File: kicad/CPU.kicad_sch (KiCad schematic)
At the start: 49 parts, among them SW1 SW_Push, U10 MC34063AD, U11 LD1117S33TR_SOT223, U4 MC34063AD, U5 STM32F303CBTx, X1 8 MHz

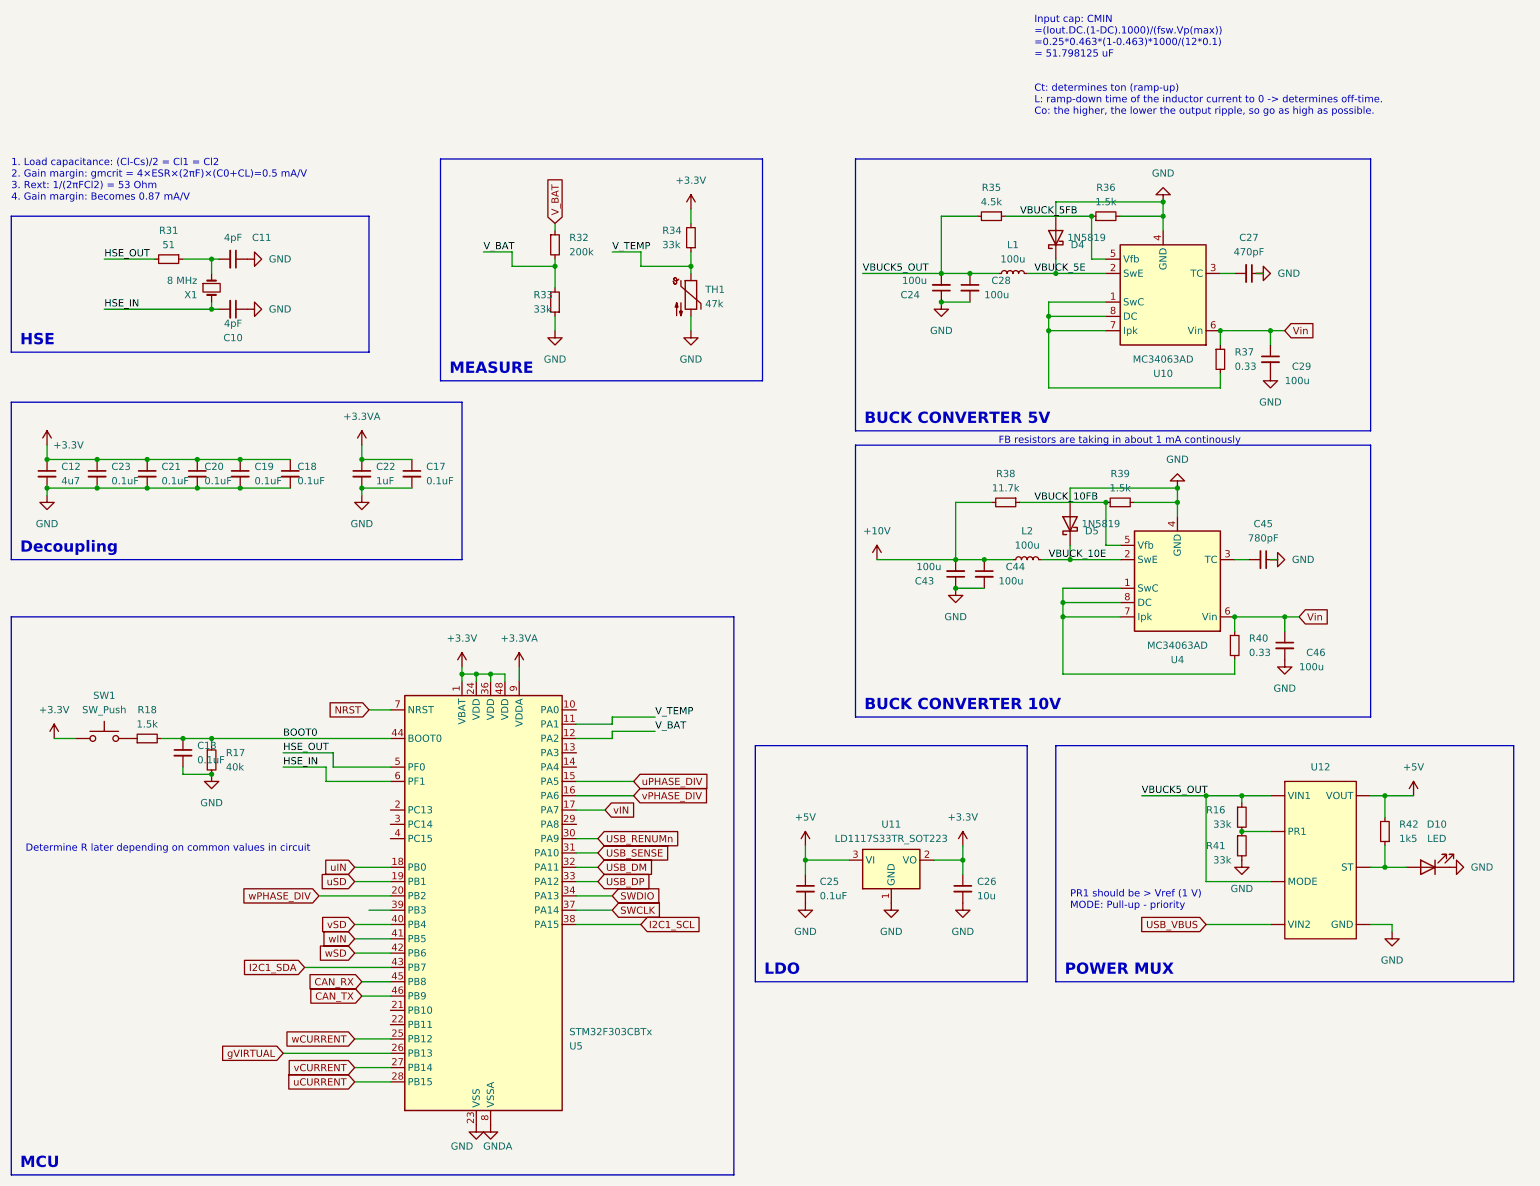
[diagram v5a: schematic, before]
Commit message: [kicad] completed resistor and capacitor BOM, added footprints, streamlined the resistance and capacitance values | TODO: find new crystal, add footprint for CAN driver + button, check IC-footprints [simulations] adapted the simulations according to changes in the schematic [scripts] Added warning for HP 0.33 ohm resistor
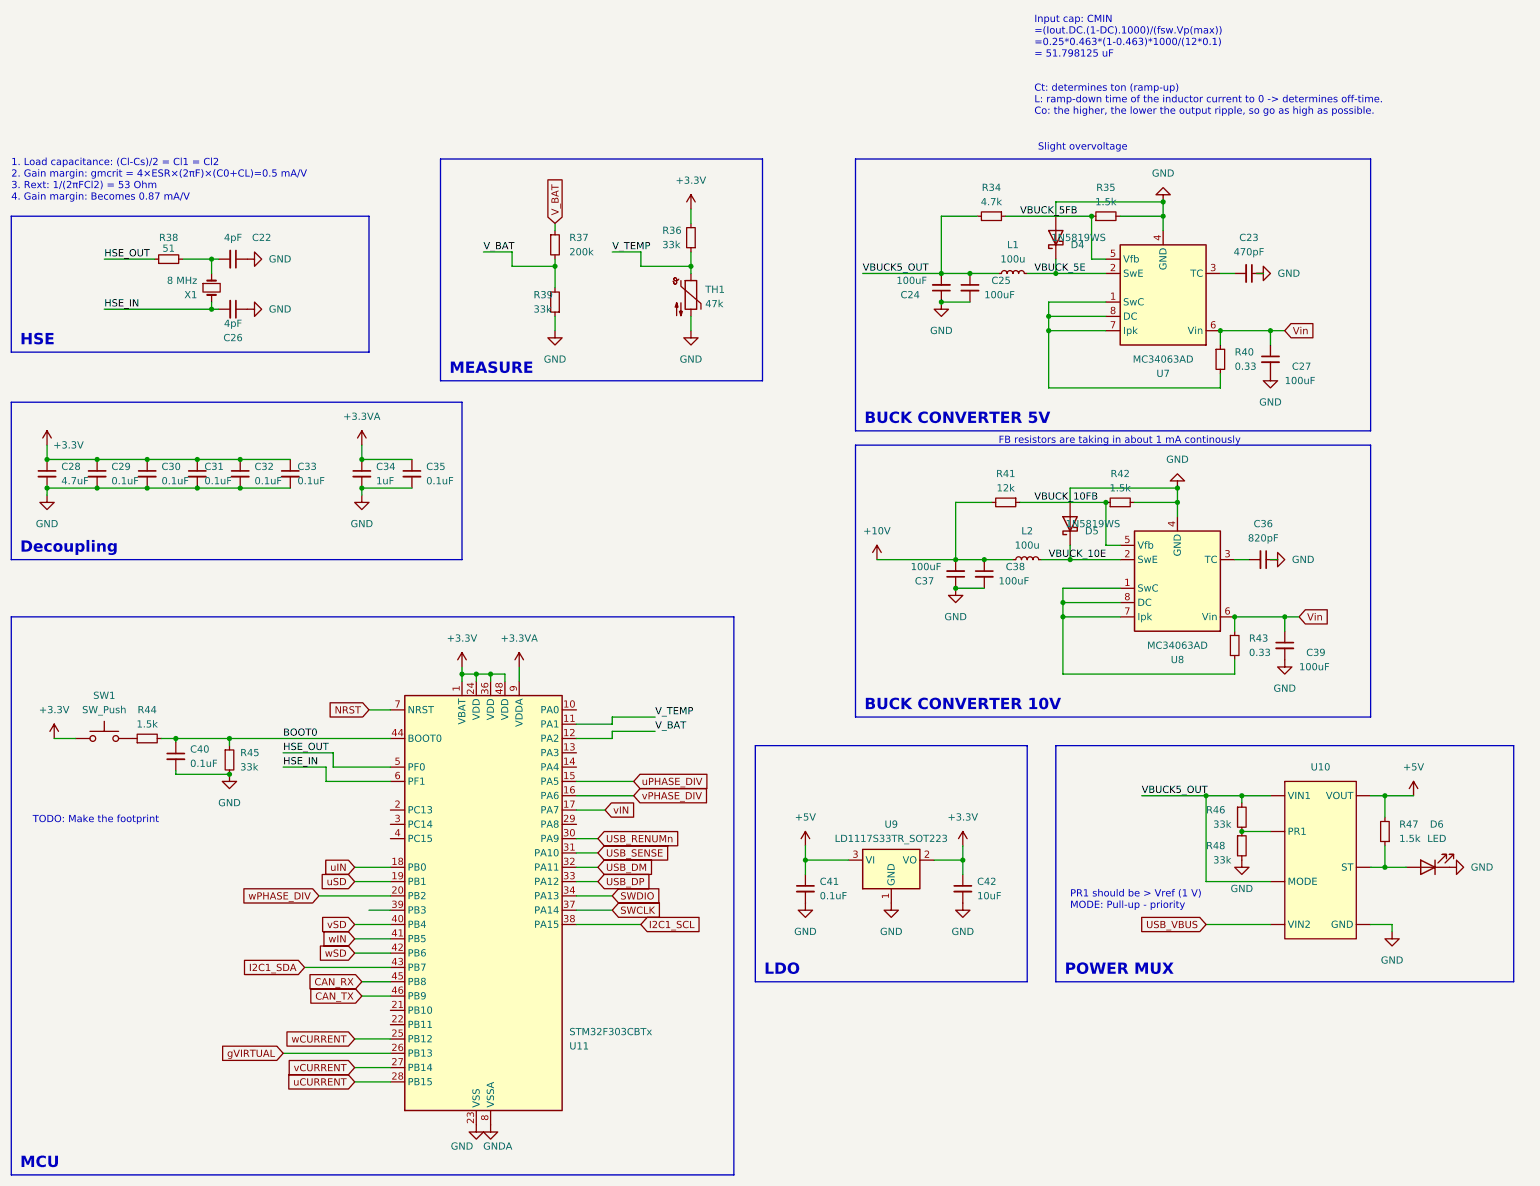
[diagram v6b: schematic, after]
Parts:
- removed R31: 51, Resistor_SMD:R_0805_2012Metric, symbol Device:R_Small
- removed R39: 1.5k, symbol Device:R_Small
- added R38: 51, Resistor_SMD:R_1206_3216Metric, symbol Device:R_Small
- added R42: 1.5k, Resistor_SMD:R_0805_2012Metric, symbol Device:R_Small
- C22: renamed from C11; footprint (none) -> Capacitor_SMD:C_0603_1608Metric; MFR.Part (none) -> CL10C040CB8NNNC; jlcpcb (none) -> C307494
- C23: renamed from C27; footprint Capacitor_SMD:C_0603_1608Metric -> Capacitor_SMD:C_0805_2012Metric; MFR.Part (none) -> 0805B471K500NT; jlcpcb (none) -> C1743
- C24: value 100u -> 100uF; MFR.Part (none) -> CA55-B6R3M107T; jlcpcb (none) -> C568913
- C25: renamed from C28; value 100u -> 100uF; MFR.Part (none) -> CA55-B6R3M107T; jlcpcb (none) -> C568913
- C26: renamed from C10; footprint (none) -> Capacitor_SMD:C_0603_1608Metric; MFR.Part (none) -> CL10C040CB8NNNC; jlcpcb (none) -> C307494
- C27: renamed from C29; value 100u -> 100uF; MFR.Part (none) -> CA55-B6R3M107T; jlcpcb (none) -> C568913
- C28: renamed from C12; value 4u7 -> 4.7uF; JLCPCB C19666 -> (none); jlcpcb (none) -> C19666
- C34: renamed from C22; jlcpcb (none) -> C1848; jlpcb C1848 -> (none)
- C36: renamed from C45; value 780pF -> 820pF; footprint Capacitor_SMD:C_0603_1608Metric -> Capacitor_SMD:C_0805_2012Metric; MFR.Part (none) -> CL21B821KBANNNC; jlcpcb (none) -> C296722
- C37: renamed from C43; value 100u -> 100uF; MFR.Part (none) -> CA55-B6R3M107T; jlcpcb (none) -> C568913
- C38: renamed from C44; value 100u -> 100uF; MFR.Part (none) -> CA55-B6R3M107T; jlcpcb (none) -> C568913
- C39: renamed from C46; value 100u -> 100uF; MFR.Part (none) -> CA55-B6R3M107T; jlcpcb (none) -> C568913
- C42: renamed from C26; value 10u -> 10uF; footprint (none) -> Capacitor_SMD:C_0402_1005Metric; jlcpcb (none) -> C15525
- D4, D5: value 1N5819 -> 1N5819WS; footprint Diode_THT:D_DO-41_SOD81_P10.16mm_Horizontal -> Diode_SMD:D_SOD-323; MFR.Part (none) -> 1N5819WS; jlcpcb (none) -> C191023
- D6: renamed from D10; MFR.Part (none) -> BZ-C0805-Y2-E1; jlcpcb (none) -> C2833070
- R34: renamed from R35; value 4.5k -> 4.7k; footprint (none) -> Resistor_SMD:R_0805_2012Metric; MFR.Part (none) -> 0805W8F4701T5E; jlcpcb (none) -> C17673
- R35: renamed from R36; footprint (none) -> Resistor_SMD:R_0805_2012Metric; jlcpcb (none) -> C4310
- R40: renamed from R37; footprint (none) -> Resistor_SMD:R_2512_6332Metric; MFR.Part (none) -> 25121WF330LT4E; jlcpcb (none) -> C25468
- R41: renamed from R38; value 11.7k -> 12k; footprint (none) -> Resistor_SMD:R_0603_1608Metric; MFR.Part (none) -> 0603WAF1202T5E; jlcpcb (none) -> C22790
- R43: renamed from R40; footprint (none) -> Resistor_SMD:R_2512_6332Metric; MFR.Part (none) -> 25121WF330LT4E; jlcpcb (none) -> C25468
- R44: renamed from R18; footprint (none) -> Resistor_SMD:R_0805_2012Metric; jlcpcb (none) -> C4310
- R45: renamed from R17; value 40k -> 33k; footprint (none) -> Resistor_SMD:R_0603_1608Metric; jlcpcb (none) -> C4216
- R46: renamed from R16; footprint (none) -> Resistor_SMD:R_0603_1608Metric; jlcpcb (none) -> C4216
- R47: renamed from R42; value 1k5 -> 1.5k; footprint (none) -> Resistor_SMD:R_0805_2012Metric; jlcpcb (none) -> C4310
- R48: renamed from R41; footprint (none) -> Resistor_SMD:R_0603_1608Metric; jlcpcb (none) -> C4216
- SW1: MFR.Part (none) -> 5.8 ZSGT; jlcpcb (none) -> C2681587
- U10: renamed from U12; footprint (none) -> Package_TO_SOT_SMD:SOT-583-8; MFR.Part (none) -> TPS2116DRLR; jlcpcb (none) -> C3235557
- renumbered C23 to C29, C21 to C30, C20 to C31, C19 to C32, C18 to C33, C17 to C35, C13 to C40, C25 to C41, R34 to R36, R32 to R37, R33 to R39, U5 to U11, U10 to U7, U4 to U8, U11 to U9
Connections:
- net GND: now also R42.2
- net HSE_OUT: now also R38.1
- net VBUCK_10FB: now also R42.1
- net at C22.2, X1.1: now also R38.2
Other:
- note added: "Slight overvoltage"
- note added: "TODO: Make the footprint"
- note removed: "Determine R later depending on common values in circuit"
- moved on the sheet: C40, R45

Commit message: [kicad] Added oscillator and relevant surrounding circuitry [scripts] Added resonator calculation
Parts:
- C22, C26: value 4pF -> 20pF; MFR.Part CL10C040CB8NNNC -> CL10C200JB81PNC; jlcpcb C307494 -> C346210
- R38: value 51 -> 0; footprint Resistor_SMD:R_1206_3216Metric -> Resistor_SMD:R_0402_1005Metric; JLCPCB (none) -> C17168; MFR.Part 1206W4F510JT5E -> 0402WGF0000TCE; jlcpcb C18019 -> (none)
- X1: footprint (none) -> Crystal:Crystal_SMD_3225-4Pin_3.2x2.5mm; Component ABLS-8.000MHZ-20-B-3-H-T -> (none); MFR.Part (none) -> 7325-0800A2010-00; jlcpcb (none) -> C389817
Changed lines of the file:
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@@
+    )
+  )
+  (symbol (lib_id "Device:C_Small") (at 53.34 33.02 270) (unit 1)
+    (in_bom yes) (on_board yes) (dnp no)
+    (property "Reference" "C22" (at 53.34 38.1 90)
+      (effects (font (size 1.27 1.27)))
+    )
+    (property "Value" "20pF" (at 53.34 35.56 90)
+      (effects (font (size 1.27 1.27)))
+    )
+    (property "Footprint" "Capacitor_SMD:C_0603_1608Metric" (at 53.34 33.02 0)
+      (effects (font (size 1.27 1.27)) hide)
+    )
+    (property "Datasheet" "https://wmsc.lcsc.com/wmsc/upload/file/pdf/v2/lcsc/2304140030_Samsung-Electro-Mechanics-CL10C040CB8NNNC_C307494.pdf" (at 53.34 33.02 0)
+      (effects (font (size 1.27 1.27)) hide)
+    )
+    (property "MFR.Part" "CL10C200JB81PNC" (at 53.34 33.02 0)
+      (effects (font (size 1.27 1.27)) hide)
+    )
+    (property "jlcpcb" "C346210" (at 53.34 33.02 0)
+      (effects (font (size 1.27 1.27)) hide)
+    )
+    (pin "1")
+    (pin "2")
+    (instances
+      (project "bldc_project"
+        (path "/91e2f46a-700b-4d7a-a06a-22469f63223f/7eb1e86b-8a48-408f-b231-0c52f4ea1971"
+          (reference "C22") (unit 1)
+        )
+      )
     )
   )
@@
     )
   )
-  (symbol (lib_id "Device:C_Small") (at 53.34 33.02 270) (unit 1)
-    (in_bom yes) (on_board yes) (dnp no)
-    (property "Reference" "C22" (at 58.42 29.21 90)
-      (effects (font (size 1.27 1.27)))
-    )
-    (property "Value" "4pF" (at 53.34 29.21 90)
-      (effects (font (size 1.27 1.27)))
-    )
-    (property "Footprint" "Capacitor_SMD:C_0603_1608Metric" (at 53.34 33.02 0)
-      (effects (font (size 1.27 1.27)) hide)
-    )
-    (property "Datasheet" "https://wmsc.lcsc.com/wmsc/upload/file/pdf/v2/lcsc/2304140030_Samsung-Electro-Mechanics-CL10C040CB8NNNC_C307494.pdf" (at 53.34 33.02 0)
-      (effects (font (size 1.27 1.27)) hide)
-    )
-    (property "MFR.Part" "CL10C040CB8NNNC" (at 53.34 33.02 0)
-      (effects (font (size 1.27 1.27)) hide)
-    )
-    (property "jlcpcb" "C307494" (at 53.34 33.02 0)
-      (effects (font (size 1.27 1.27)) hide)
-    )
-    (pin "1")
-    (pin "2")
-    (instances
-      (project "bldc_project"
-        (path "/91e2f46a-700b-4d7a-a06a-22469f63223f/7eb1e86b-8a48-408f-b231-0c52f4ea1971"
-          (reference "C22") (unit 1)
-        )
-      )
-    )
-  )
   (symbol (lib_id "Device:C_Small") (at 38.1 71.12 0) (unit 1)
     (in_bom yes) (on_board yes) (dnp no) (fields_autoplaced)
@@
       (effects (font (size 1.27 1.27)))
     )
-    (property "Value" "4pF" (at 53.34 44.45 90)
+    (property "Value" "20pF" (at 53.34 44.45 90)
       (effects (font (size 1.27 1.27)))
     )
@@
       (effects (font (size 1.27 1.27)) hide)
     )
-    (property "Datasheet" "https://wmsc.lcsc.com/wmsc/upload/file/pdf/v2/lcsc/2304140030_Samsung-Electro-Mechanics-CL10C040CB8NNNC_C307494.pdf" (at 53.34 41.91 0)
-      (effects (font (size 1.27 1.27)) hide)
-    )
-    (property "MFR.Part" "CL10C040CB8NNNC" (at 53.34 41.91 0)
-      (effects (font (size 1.27 1.27)) hide)
-    )
-    (property "jlcpcb" "C307494" (at 53.34 41.91 0)
+    (property "Datasheet" "https://wmsc.lcsc.com/wmsc/upload/file/pdf/v2/lcsc/2304140030_Samsung-Electro-Mechanics-CL10C200JB81PNC_C346210.pdf" (at 53.34 41.91 0)
+      (effects (font (size 1.27 1.27)) hide)
+    )
+    (property "MFR.Part" "CL10C200JB81PNC" (at 53.34 41.91 0)
+      (effects (font (size 1.27 1.27)) hide)
+    )
+    (property "jlcpcb" "C346210" (at 53.34 41.91 0)
       (effects (font (size 1.27 1.27)) hide)
     )
@@
       (effects (font (size 1.27 1.27)) (justify right))
     )
-    (property "Footprint" "" (at 49.53 38.1 0)
-      (effects (font (size 1.27 1.27)) hide)
-    )
-    (property "Datasheet" "https://4donline.ihs.com/images/VipMasterIC/IC/ABRC/ABRCS03441/ABRCS03441-1.pdf?hkey=6D3A4C79FDBF58556ACFDE234799DDF0" (at 49.53 38.1 0)
-      (effects (font (size 1.27 1.27)) hide)
-    )
-    (property "Component" "ABLS-8.000MHZ-20-B-3-H-T" (at 49.53 38.1 90)
+    (property "Footprint" "Crystal:Crystal_SMD_3225-4Pin_3.2x2.5mm" (at 49.53 38.1 0)
+      (effects (font (size 1.27 1.27)) hide)
+    )
+    (property "Datasheet" "https://wmsc.lcsc.com/wmsc/upload/file/pdf/v2/lcsc/1912111437_XTY-7325-0800A2010-00_C389817.pdf" (at 49.53 38.1 0)
+      (effects (font (size 1.27 1.27)) hide)
+    )
+    (property "jlcpcb" "C389817" (at 49.53 38.1 90)
+      (effects (font (size 1.27 1.27)) hide)
+    )
+    (property "MFR.Part" "7325-0800A2010-00" (at 49.53 38.1 90)
       (effects (font (size 1.27 1.27)) hide)
     )
@@
       (effects (font (size 1.27 1.27)))
     )
-    (property "Value" "51" (at 41.91 31.115 90)
-      (effects (font (size 1.27 1.27)))
-    )
-    (property "Footprint" "Resistor_SMD:R_1206_3216Metric" (at 41.91 33.02 0)
-      (effects (font (size 1.27 1.27)) hide)
-    )
-    (property "Datasheet" "https://wmsc.lcsc.com/wmsc/upload/file/pdf/v2/lcsc/2206010145_UNI-ROYAL-Uniroyal-Elec-1206W4F510JT5E_C18019.pdf" (at 41.91 33.02 0)
-      (effects (font (size 1.27 1.27)) hide)
-    )
-    (property "JLCPCB" "" (at 41.91 33.02 90)
-      (effects (font (size 1.27 1.27)) hide)
-    )
-    (property "MFR.Part" "1206W4F510JT5E" (at 41.91 33.02 90)
-      (effects (font (size 1.27 1.27)) hide)
-    )
-    (property "jlcpcb" "C18019" (at 41.91 33.02 0)
-      (effects (font (size 1.27 1.27)) hide)
-    )
+    (property "Value" "0" (at 41.91 31.115 90)
+      (effects (font (size 1.27 1.27)))
+    )
+    (property "Footprint" "Resistor_SMD:R_0402_1005Metric" (at 41.91 33.02 0)
+      (effects (font (size 1.27 1.27)) hide)
+    )
+    (property "Datasheet" "https://wmsc.lcsc.com/wmsc/upload/file/pdf/v2/lcsc/2206010216_UNI-ROYAL-Uniroyal-Elec-0402WGF0000TCE_C17168.pdf" (at 41.91 33.02 0)
+      (effects (font (size 1.27 1.27)) hide)
+    )
+    (property "JLCPCB" "C17168" (at 41.91 33.02 90)
+      (effects (font (size 1.27 1.27)) hide)
+    )
+    (property "MFR.Part" "0402WGF0000TCE" (at 41.91 33.02 90)
+      (effects (font (size 1.27 1.27)) hide)
+    )
